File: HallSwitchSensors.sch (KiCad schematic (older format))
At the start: 28 parts, among them K1 CONN_3, K2 CONN_3, K3 CONN_3, K4 CONN_3

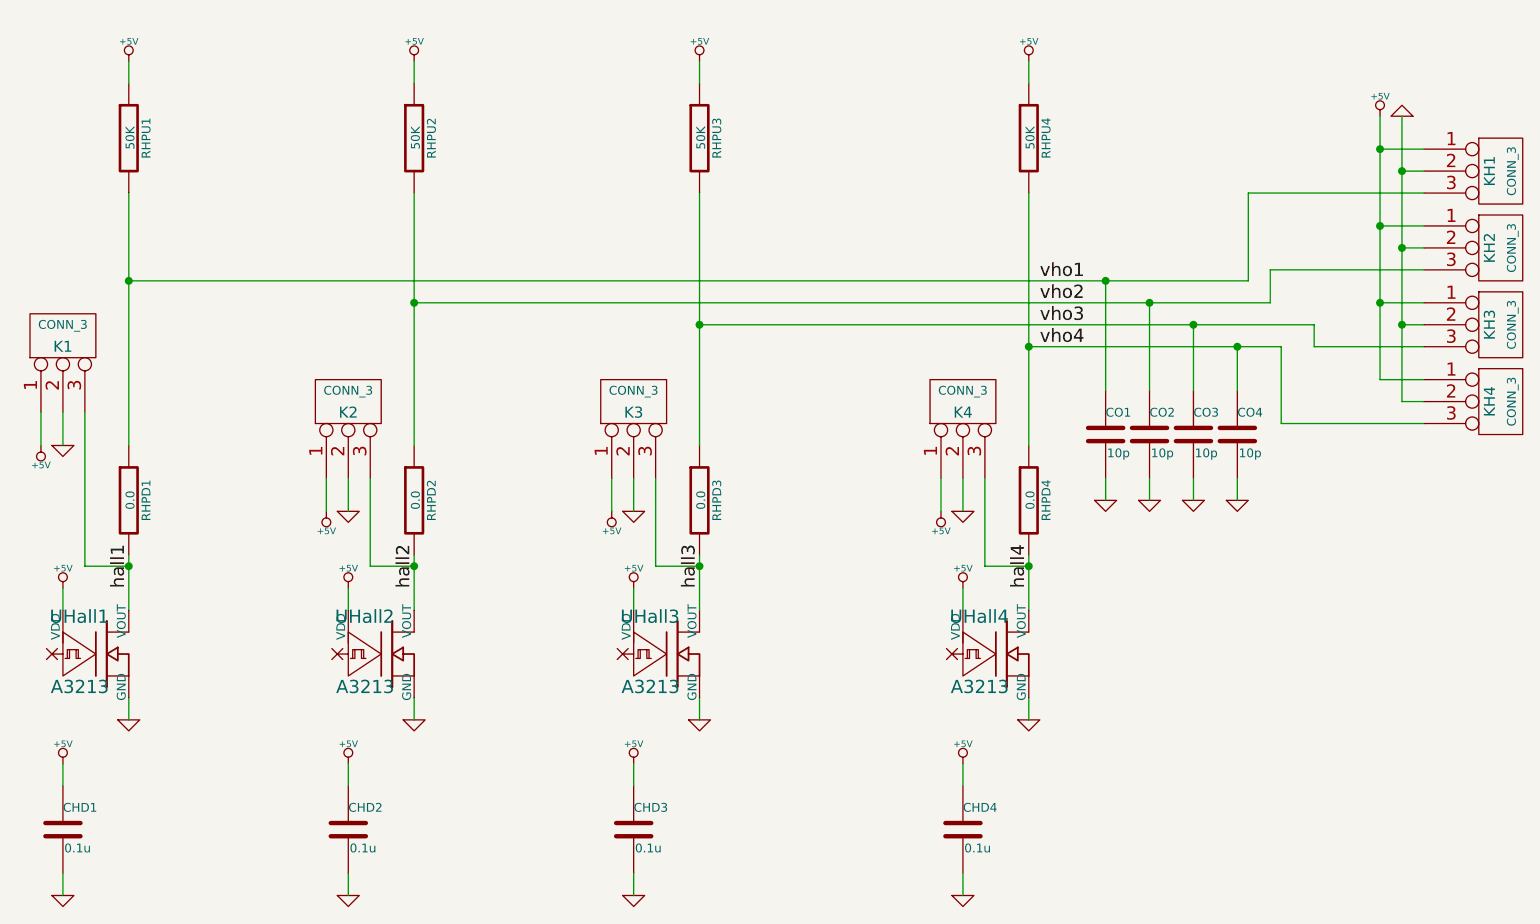
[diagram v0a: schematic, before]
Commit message: Reworking as multi-schematic hierarchy.  Doesn't look like kicad is truly hierarchical in the one-master to many-instances sense, but still investigating.
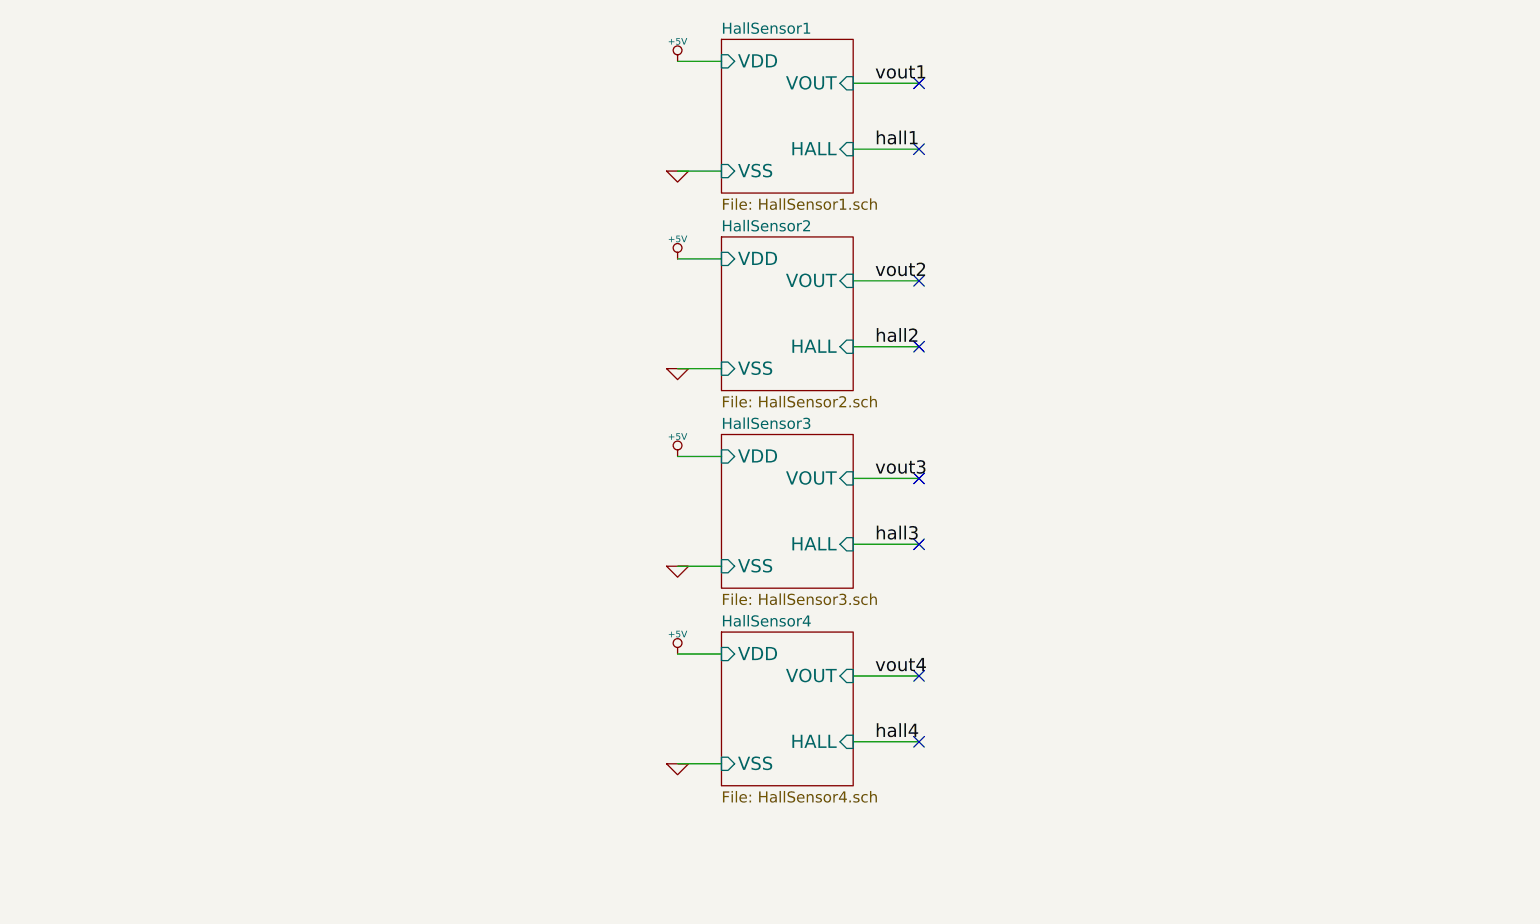
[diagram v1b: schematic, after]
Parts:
- removed CHD1, CHD2, CHD3, CHD4: 0.1u, ~, symbol C
- removed CO1, CO2, CO3, CO4: 10p, ~, symbol C
- removed K1, K2, K3, K4, KH1, KH2, KH3, KH4: CONN_3, symbol CONN_3
- removed RHPD1, RHPD2, RHPD3, RHPD4: 0.0, ~, symbol R
- removed RHPU1, RHPU2, RHPU3, RHPU4: 50K, ~, symbol R
- removed UHall1, UHall2, UHall3, UHall4: A3213, ~, symbol A3213
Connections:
- no-connect marks 0 -> 8
